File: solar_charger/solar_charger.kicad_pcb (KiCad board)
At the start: 4 copper layers, 78.9 x 59.4 mm, 12 parts, among them J1 Screw_Terminal_01x02, J2 Screw_Terminal_01x02, J3 Screw_Terminal_01x02, J4 Screw_Terminal_01x02, J5 Conn_02x20_Odd_Even, J6 Screw_Terminal_01x02, U1 INA260, U2 INA260, U3 INA260

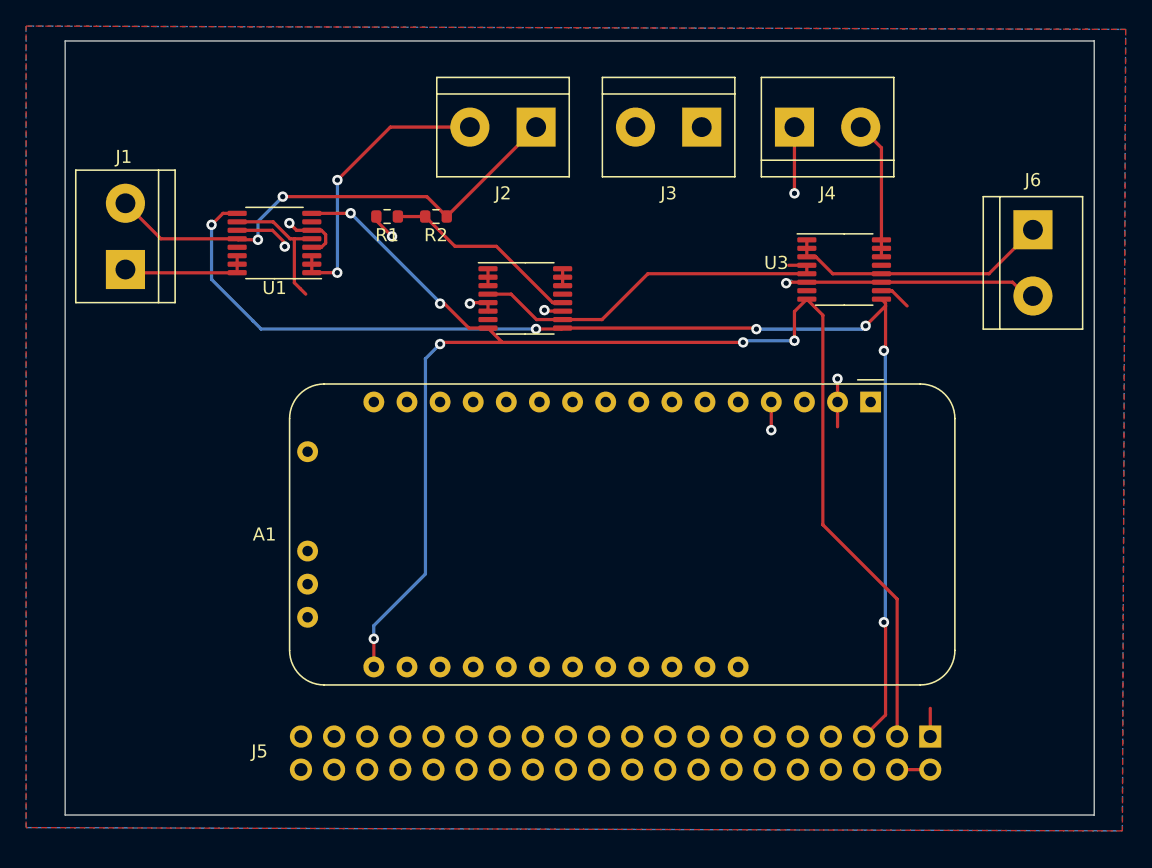
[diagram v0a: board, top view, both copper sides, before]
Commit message: edited silkscreen of solar charger circuit
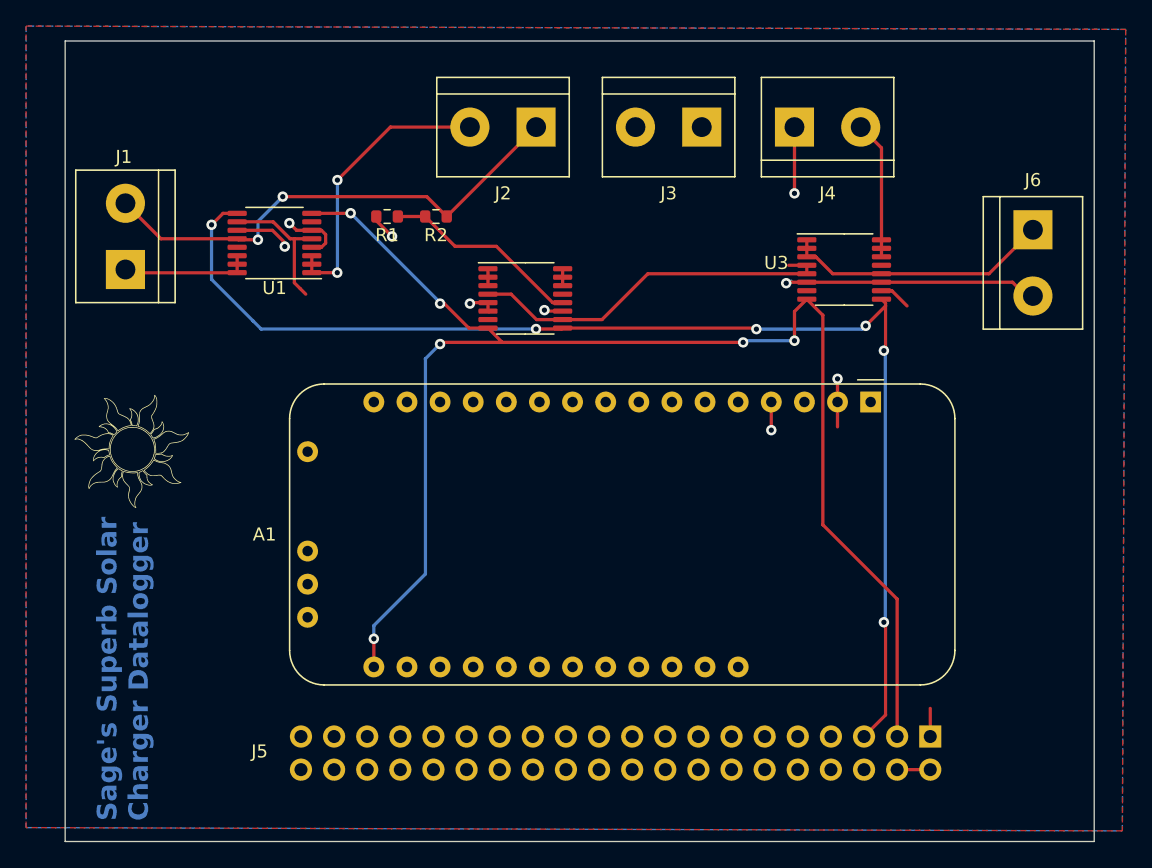
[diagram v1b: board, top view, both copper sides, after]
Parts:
- added G***: LOGO, LOGO, F.Cu at (104.1, 67.9)
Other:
- board size 78.9 x 59.4 mm -> 78.9 x 61.4 mm
- board text added: "Sage's Superb Solar Charger Datalogger"

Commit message: made board review changes
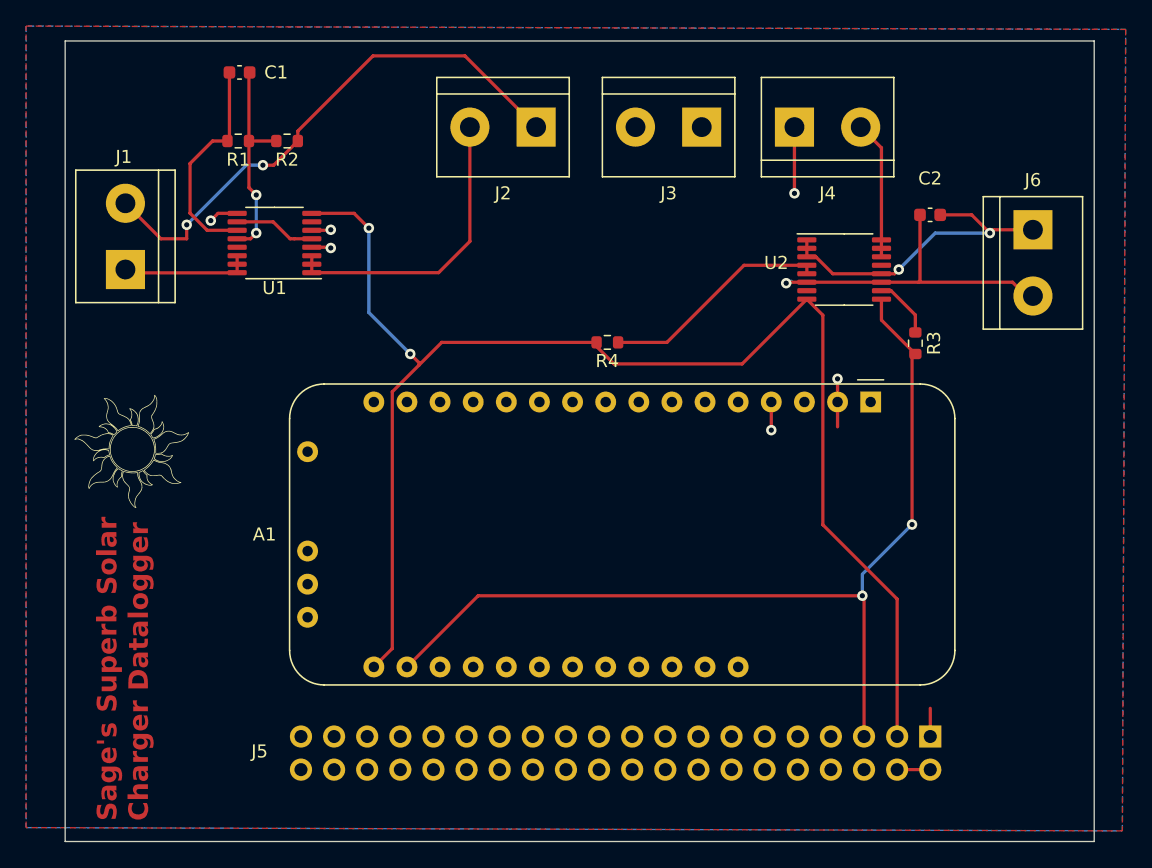
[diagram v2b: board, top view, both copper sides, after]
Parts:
- removed the U2 at (134.3, 56.3)
- added C1: 0.1u, Capacitor_SMD:C_0603_1608Metric, F.Cu at (112.4, 39.0)
- added C2: 0.1u, Capacitor_SMD:C_0603_1608Metric, F.Cu at (165.3, 49.9)
- added R3: 10k, Resistor_SMD:R_0603_1608Metric, F.Cu at (164.2, 59.8)
- added R4: 10k, Resistor_SMD:R_0603_1608Metric, F.Cu at (140.6, 59.7)
- moved R1 12.8 mm to (112.3, 44.2)
- moved R2 12.8 mm to (116.0, 44.2)
- renumbered U3 to U2
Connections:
- R1 pad 1: Net-(U2-VBUS) -> Net-(U1-VBUS)
- R2 pad 2: Net-(U2-VBUS) -> Net-(U1-VBUS)
- U1 pad 12: /+V_SOLAR -> Net-(U1-VBUS)
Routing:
- net Net-(U1-VBUS): track 0.00 -> 15.9 mm, vias 0 -> 2
- net Net-(U2-VBUS): track 15.4 -> 0.00 mm
- net 3V3: track 48.3 -> 34.8 mm
- net GND: track 42.6 -> 52.4 mm, vias 8 -> 5
- net SCL: track 125.1 -> 116.3 mm, vias 6 -> 3
- net /+V_BATT: track 20.6 -> 26.0 mm, vias 0 -> 2
- net /+V_SOLAR: track 38.3 -> 41.8 mm
- net SDA: track 112.9 -> 111.3 mm, vias 6 -> 2
- net unconnected-(U2-IN--Pad14): track 1.30 -> 0.00 mm
- net unconnected-(U2-IN+-Pad1): track 1.30 -> 0.00 mm
- net /-V_SOLAR_CHG: track 22.2 -> 23.2 mm, vias 2 -> 0

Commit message: changed screw terminal footprint
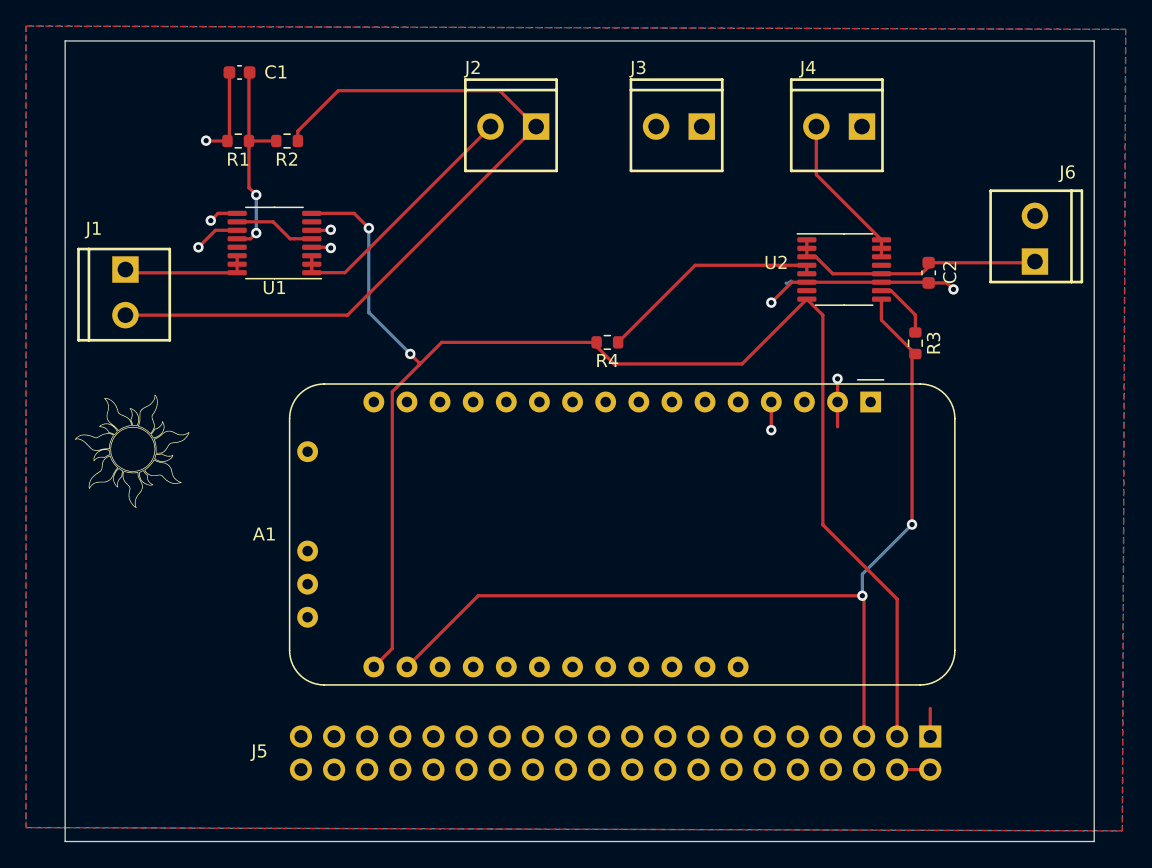
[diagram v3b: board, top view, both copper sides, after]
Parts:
- removed the G*** at (104.1, 67.9)
- added G***: SUN, mainboard:SUN, F.Cu at (104.2, 67.9)
- J1, J2, J3, J4, J6: footprint TerminalBlock:TerminalBlock_bornier-2_P5.08mm -> mainboard:SCREWTERMINAL-3.5MM-2_LOCK
- moved J4 5.18 mm to (160.1, 43.1), turned to 180 degrees
- moved C2 4.45 mm to (165.2, 54.4), turned to -90 degrees
- moved J6 2.44 mm to (173.4, 53.5), turned to 90 degrees
- turned J1 to -90 degrees
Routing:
- net GND: track 52.4 -> 31.2 mm, vias 5 -> 7
- net /+V_SOLAR: track 41.8 -> 59.0 mm, vias 2 -> 0
- net /+V_BATT: track 26.0 -> 19.9 mm, vias 2 -> 0
- net /-V_SOLAR_CHG: track 23.2 -> 19.6 mm
- net /+V_SOLAR_CHG: track 10.6 -> 12.1 mm
- net CHG: track 74.7 -> 75.4 mm
